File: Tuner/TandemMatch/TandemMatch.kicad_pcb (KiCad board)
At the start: 2 copper layers, 100 x 100 mm, 118 parts, among them J10 Conn_01x01, J11 Conn_01x01, J12 Conn_01x01, J13 Conn_01x01, J14 Conn_01x01, J15 Conn_01x01, J16 Conn_01x01, J18 Conn_Coaxial, J20 Conn_Coaxial, J21 Conn_01x01, J22 Conn_01x01, J23 Conn_01x01, J24 Conn_01x01, J25 Conn_01x01, J26 Conn_01x01, J27 Conn_01x01, J28 Conn_01x01, J29 Conn_01x01, J3 Conn_Coaxial, J30 Conn_01x01, J31 Conn_01x01, J32 Conn_01x01, J33 Conn_01x03, J34 Conn_01x01, J35 Conn_01x01, J36 Conn_01x01, J37 Conn_01x01, J38 Conn_01x01, J39 Conn_01x01, J4 Conn_Coaxial, J40 Conn_01x01, J41 Conn_01x01, J42 Conn_Coaxial, J43 Conn_Coaxial, J44 Conn_01x01, J45 Conn_01x01, J46 Conn_01x01, J47 Conn_01x01, J48 Conn_01x01, J49 Conn_01x01, J5 Conn_01x01, J50 Conn_01x01, J51 Conn_01x01, J52 Conn_01x01, J53 Conn_01x01, J54 Conn_01x01, J55 Conn_01x01, J56 Conn_01x01, J57 Conn_01x01, J58 Conn_01x01, J59 Conn_01x01, J6 Conn_01x01, J60 Conn_Coaxial, J61 Conn_Coaxial, J62 Conn_01x04, J63 Conn_01x01, J64 Conn_01x01, J65 Conn_01x01, J66 Conn_01x01, J7 Conn_01x01, J8 Conn_01x01, J9 Conn_01x01

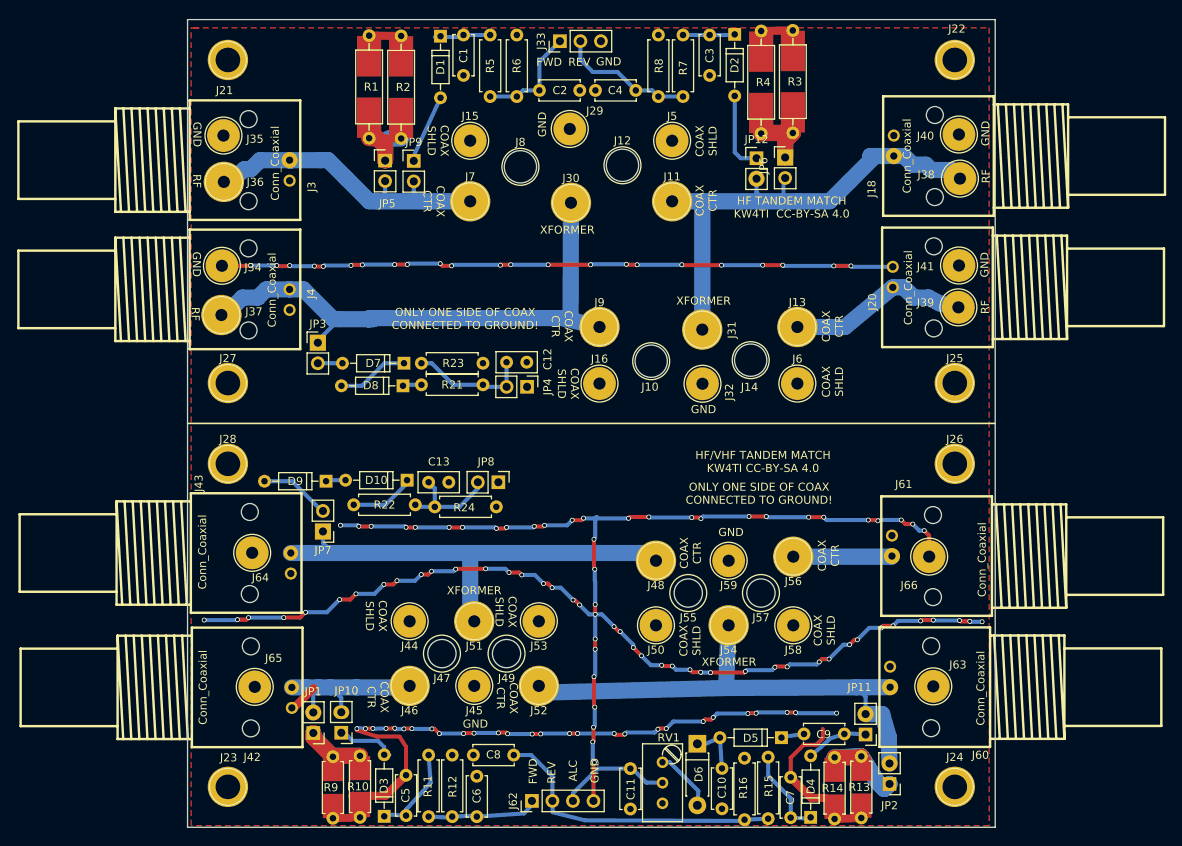
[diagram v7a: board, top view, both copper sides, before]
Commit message: TandenMatch now has DC-RF bias tee
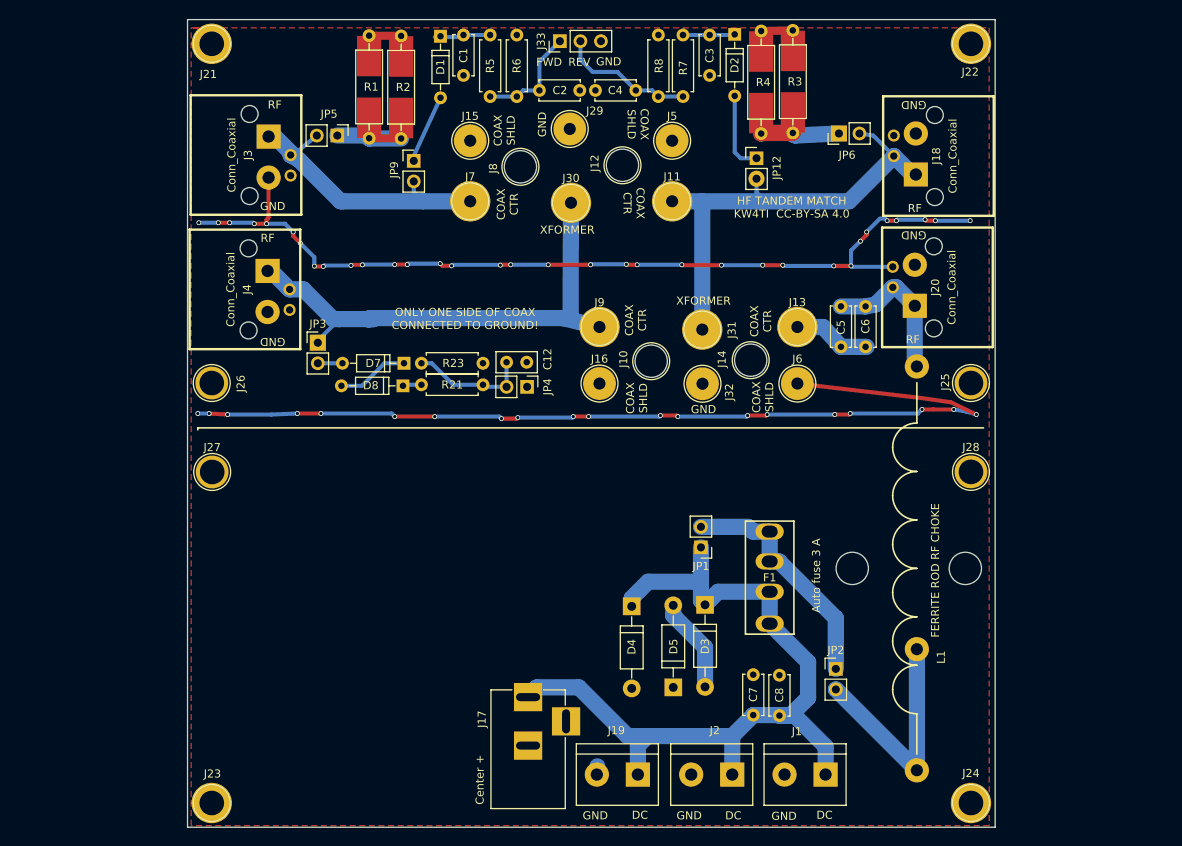
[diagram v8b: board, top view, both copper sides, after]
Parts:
- removed C10, C11: 100 nF, Capacitors_THT:C_Disc_D5.0mm_W2.5mm_P5.00mm
- removed C13: 10 nF, Capacitors_THT:C_Disc_D5.0mm_W2.5mm_P2.50mm
- removed C9: 10 nF, Capacitors_THT:C_Disc_D5.0mm_W2.5mm_P5.00mm
- removed D10, D9: 1N4148, Diodes_THT:D_DO-35_SOD27_P7.62mm_Horizontal
- removed D6: 1N4148, Diodes_THT:D_DO-41_SOD81_P7.62mm_Horizontal
- removed J34, J35, J36, J37, J38, J39, J40, J41, J44, J45, J46, J47, J48, J49, J50, J51, J52, J53, J54, J55, J56, J57, J58, J59, J63, J64, J65, J66: Conn_01x01, Connectors:1pin
- removed J42, J43, J60, J61: Conn_Coaxial, TandemMatch:bnc_90_1-1337543-0
- removed J62: Conn_01x04, Pin_Headers:Pin_Header_Straight_1x04_Pitch2.54mm
- removed JP10, JP11, JP7, JP8: Jumper_NC_Small, Pin_Headers:Pin_Header_Straight_1x02_Pitch2.54mm
- removed R10, R13, R14, R9: 100R, TandemMatch:R_Axial_DIN0207_L6.3mm_D2.5mm_P7.62mm_Horizontal_SMD
- removed R11, R12, R15, R16, R22: 10k, Resistors_THT:R_Axial_DIN0207_L6.3mm_D2.5mm_P7.62mm_Horizontal
- removed R24: 1k, Resistors_THT:R_Axial_DIN0207_L6.3mm_D2.5mm_P7.62mm_Horizontal
- removed RV1: 10k, Potentiometers:Potentiometer_Trimmer_Bourns_3296W
- added F1: Keystone 3544-2 / SL-506P, TandemMatch:SL506Pfuseholder, F.Cu at (112.1, 109.1)
- added J1: Conn_01x02, Connectors_Terminal_Blocks:TerminalBlock_bornier-2_P5.08mm, F.Cu at (119.0, 133.5)
- added J17: Barrel_Jack, Connectors:BARREL_JACK, F.Cu at (82.2, 123.9)
- added J19: Conn_01x02, Connectors_Terminal_Blocks:TerminalBlock_bornier-2_P5.08mm, F.Cu at (95.8, 133.5)
- added J2: Conn_01x02, Connectors_Terminal_Blocks:TerminalBlock_bornier-2_P5.08mm, F.Cu at (107.4, 133.5)
- added L1: L, TandemMatch:BigRFChokeInductor, F.Cu at (130.3, 108.0)
- D3: value 1N5711 -> D_Zener; footprint Diodes_THT:D_DO-35_SOD27_P7.62mm_Horizontal -> Diodes_THT:D_DO-41_SOD81_P10.16mm_Horizontal
- D4, D5: value 1N5711 -> 1N4004; footprint Diodes_THT:D_DO-35_SOD27_P7.62mm_Horizontal -> Diodes_THT:D_DO-41_SOD81_P10.16mm_Horizontal
- J18, J20, J3, J4: footprint TandemMatch:bnc_90_1-1337543-0 -> TandemMatch:bnc_90_1-1337543-0_pad_combo
- moved J26 92.5 mm to (43.0, 85.0)
- moved J28 92.0 mm to (137.0, 96.0)
- moved C5 79.2 mm to (120.9, 80.5)
- moved C6 75.5 mm to (124.0, 80.5)
- moved JP1 53.2 mm to (103.6, 105.3)
- moved D3 47.6 mm to (104.1, 112.5), turned to 270 degrees
- moved D4 34.3 mm to (95.0, 112.6), turned to 270 degrees
- moved C8 33.3 mm to (113.3, 126.2), turned to 90 degrees
- moved JP2 15.7 mm to (120.3, 120.4), turned to 0 degrees
- moved D5 14.8 mm to (100.1, 122.7), turned to 90 degrees
- moved C7 13.5 mm to (110.0, 126.1)
- moved J27 11.2 mm to (43.1, 96.0)
- moved JP6 7.29 mm to (120.7, 54.1), turned to 90 degrees
- moved JP5 6.68 mm to (58.5, 54.4), turned to 270 degrees
- moved J21 2.83 mm to (43.0, 43.0)
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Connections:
- C5 pad 2: GND -> Net-(C5-Pad2)
- C6 pad 1: Net-(C6-Pad1) -> Net-(C5-Pad1)
- C6 pad 2: GND -> Net-(C5-Pad2)
- C8 pad 1: Net-(C8-Pad1) -> Net-(C7-Pad1)
- D3 pad 1: Net-(C5-Pad1) -> Net-(C7-Pad1)
- D4 pad 2: Net-(C9-Pad2) -> GND
- D5 pad 1: Net-(C9-Pad1) -> GND
- D5 pad 2: Net-(C10-Pad1) -> Net-(D3-Pad2)
- J13 pad 1: Net-(J13-Pad1) -> Net-(C5-Pad1)
- J20 pad 1: Net-(J13-Pad1) -> Net-(C5-Pad2)
- JP1 pad 1: Net-(JP1-Pad1) -> Net-(C7-Pad1)
- JP1 pad 2: Net-(J42-Pad1) -> Net-(F1-Pad2)
- JP2 pad 1: Net-(JP2-Pad1) -> Net-(F1-Pad2)
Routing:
- net GND: track 436.8 -> 253.2 mm, vias 130 -> 54
- net Net-(C7-Pad1): track 11.6 -> 102.5 mm
- net Net-(J43-Pad1): track 57.5 -> 0.00 mm
- net Net-(C8-Pad1): track 37.3 -> 0.00 mm
- net Net-(JP2-Pad2): track 63.7 -> 29.2 mm
- net Net-(F1-Pad2): track 0.00 -> 29.8 mm
- net Net-(JP2-Pad1): track 25.2 -> 0.00 mm
- net Net-(J13-Pad1): track 22.5 -> 0.00 mm
- net Net-(J42-Pad1): track 20.9 -> 0.00 mm
- net Net-(JP1-Pad1): track 20.8 -> 0.00 mm
- net Net-(C5-Pad2): track 0.00 -> 19.3 mm
- net Net-(C11-Pad1): track 14.5 -> 0.00 mm
- net Net-(C6-Pad1): track 14.0 -> 0.00 mm
- net Net-(C13-Pad1): track 13.2 -> 0.00 mm
- net Net-(J56-Pad1): track 12.2 -> 0.00 mm
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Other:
- board text added: "Auto fuse 3 A"
- board text added: "Center +"
- board text added: "DC"
- board text added: "FERRITE ROD RF CHOKE"
- board text removed: "ALC"
- board text removed: "HF/VHF TANDEM MATCH KW4TI CC-BY-SA 4.0"
